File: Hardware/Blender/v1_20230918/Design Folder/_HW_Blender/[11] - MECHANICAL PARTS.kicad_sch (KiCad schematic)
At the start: 9 parts

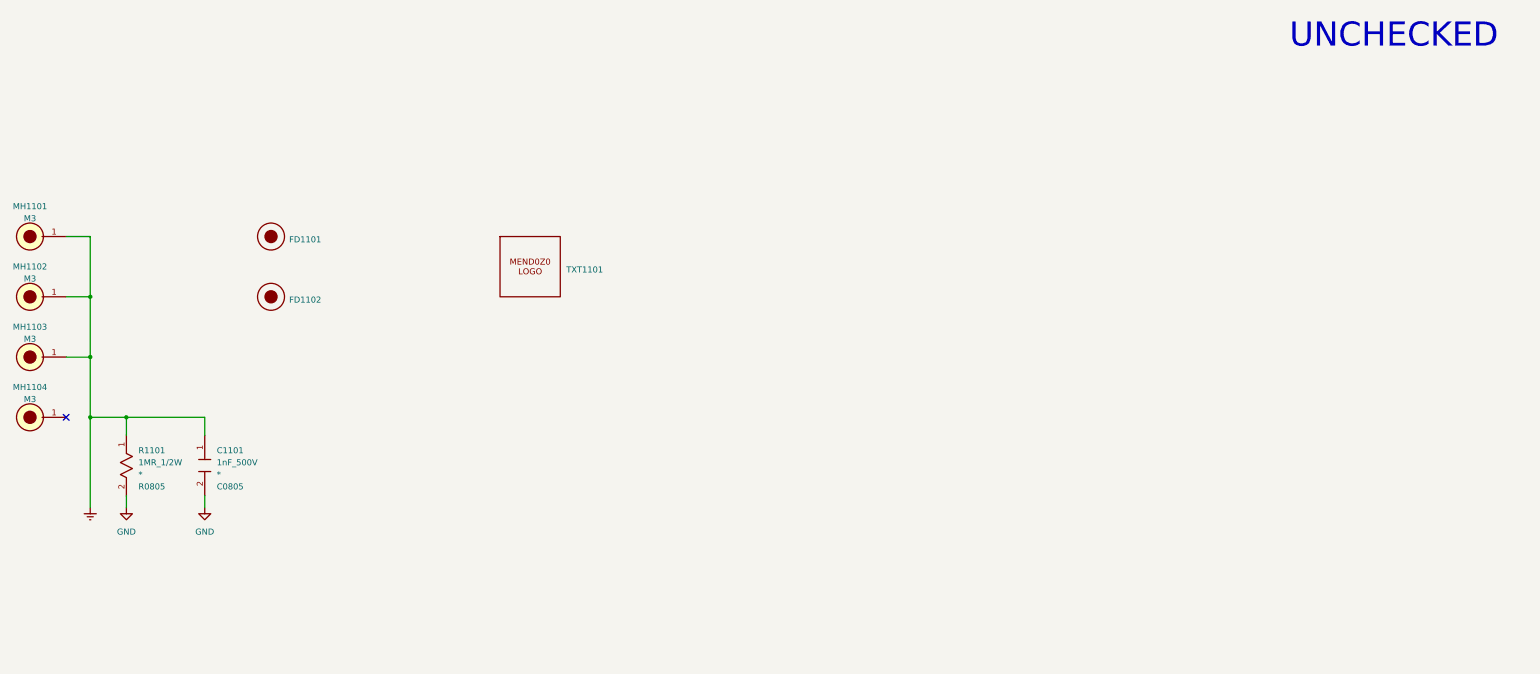
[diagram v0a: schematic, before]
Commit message: Improving the file structure and documentation
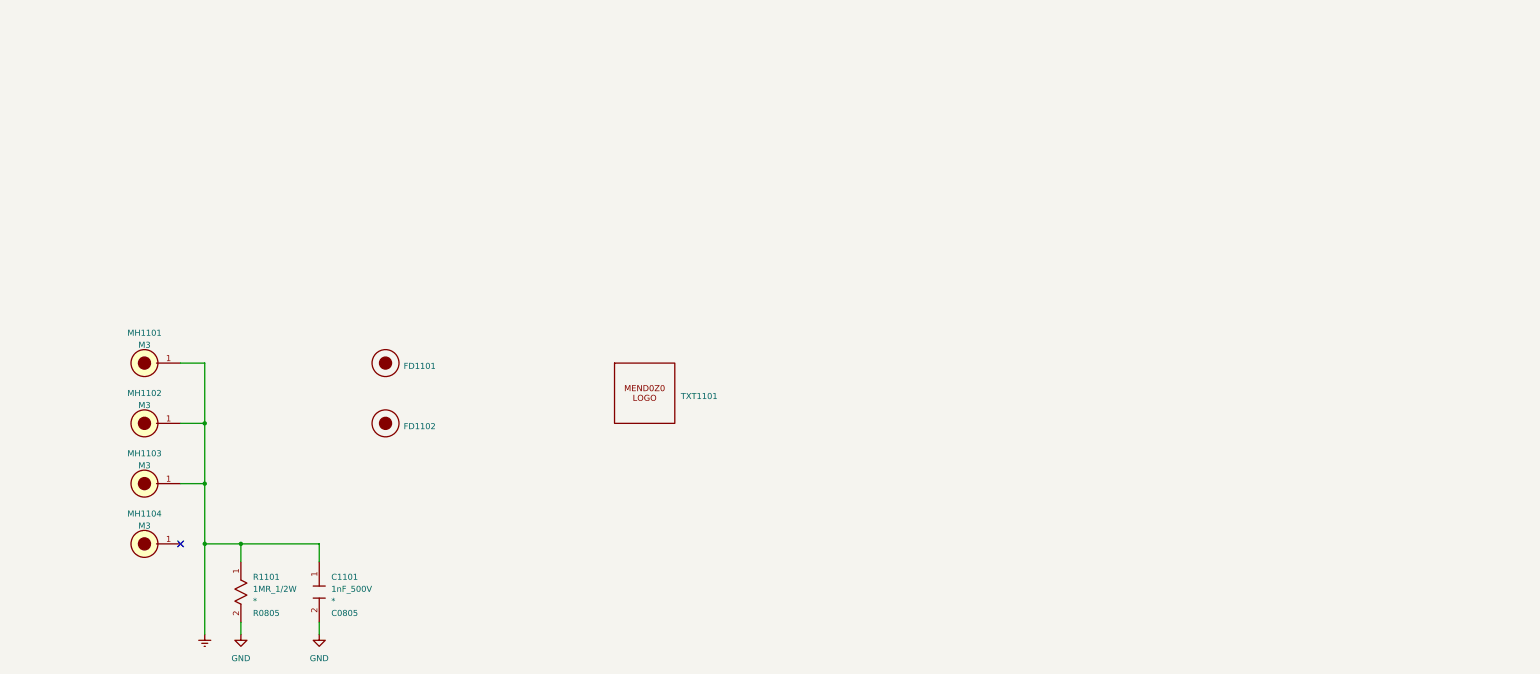
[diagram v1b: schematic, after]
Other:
- note removed: "UNCHECKED"
- moved on the sheet: C1101, FD1101, FD1102, MH1101, MH1102, MH1103, MH1104, R1101, TXT1101

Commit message: More update for hardware part
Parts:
- C1101: value 1nF_500V -> 1nF_500V_X7R; symbol _SCHLIB_Blender:CAP_1nF_500V_C0805 -> _SCHLIB_Blender:CAP_1nF_500V_X7R_C0805; Manufacturer (none) -> Würth Elektronik; PCB CHECK (none) -> PCB (N/A); Part Number 885342207013 -> (none); Part Number (Manufacturer) (none) -> 885342207013; Part Number (Vendor) (none) -> 732-12159-2-ND; SCH CHECK * -> SCH (N/A); Vendor (none) -> Digikey
- R1101: value 1MR_1/2W -> 1MR_1/2W_5%; symbol _SCHLIB_Blender:RES_1MR_1/2W_R0805 -> _SCHLIB_Blender:RES_1MR_1/2W_5%_R0805; Link https://industrial.panasonic.com/cdbs/www-data/pdf/RDO0000/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 -> https://www.digikey.ca/en/products/detail/panasonic-electro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; Manufacturer (none) -> Panasonic Electronic Components; PCB CHECk (none) -> PCB (N/A); Part Number ERJ-P06J105V -> (none); Part Number (Manufacturer) (none) -> ERJ-P06J105V; Part Number (Vendor) (none) -> P1.0MADTR-ND; SCH CHECK * -> SCH (N/A); Vendor (none) -> Digikey
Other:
- moved on the sheet: C1101
